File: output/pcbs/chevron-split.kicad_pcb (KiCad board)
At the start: 2 copper layers, 167.5 x 131.1 mm, 132 parts

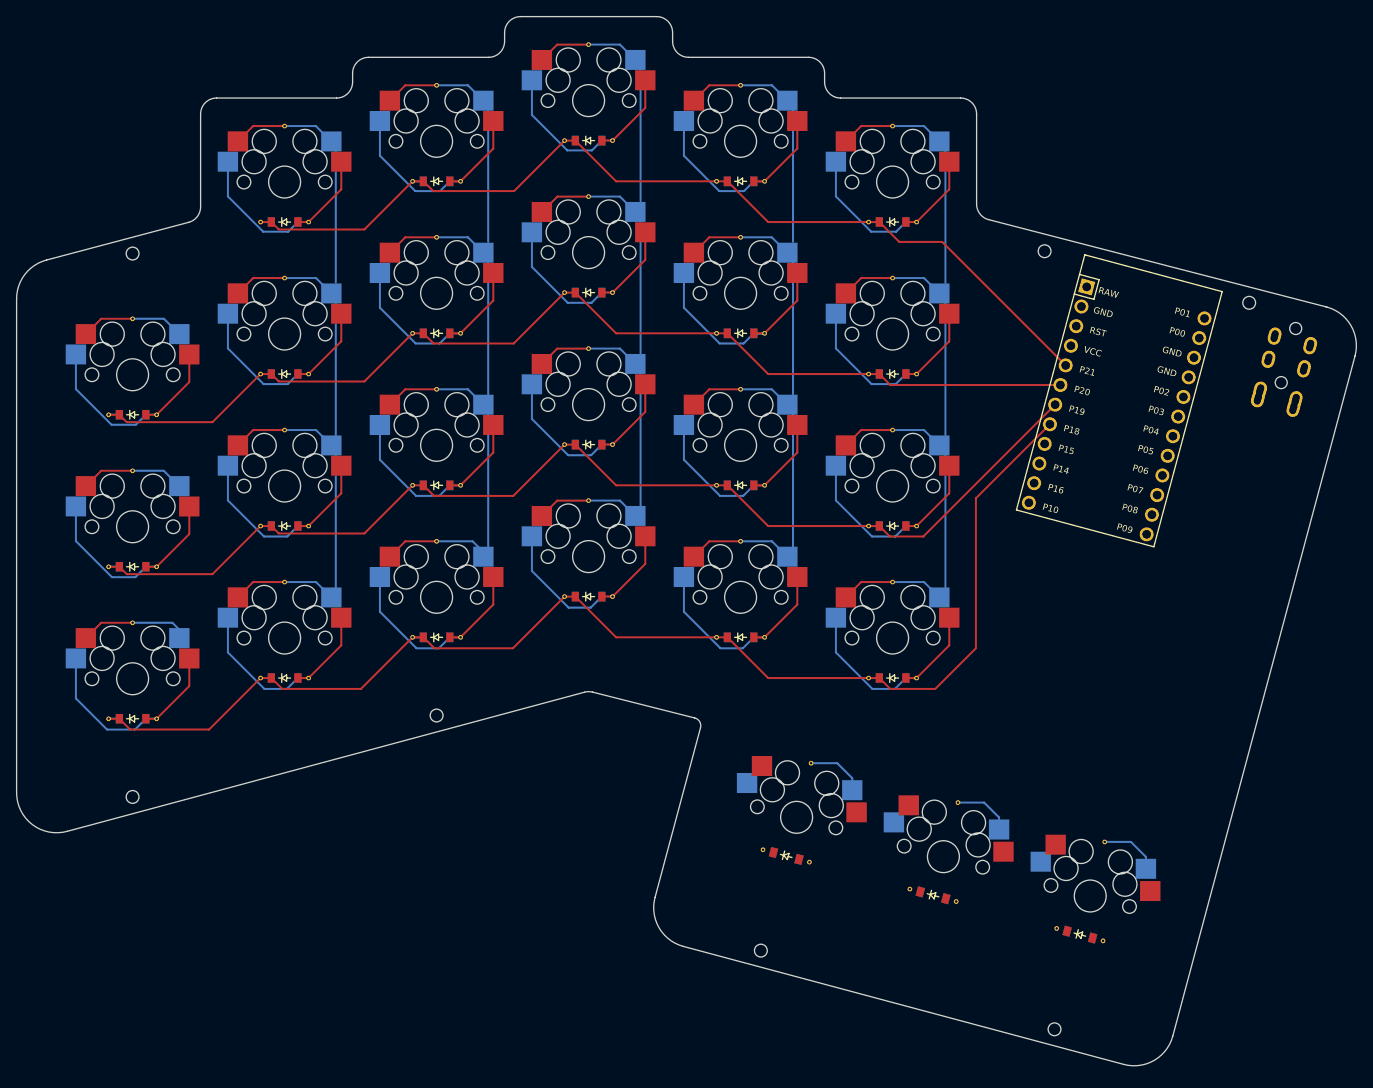
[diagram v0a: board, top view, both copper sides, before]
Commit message: Snapshot of files for manufacturing prototype version 0.1 PCBs. Created left and right versions for faster prototype iteration.
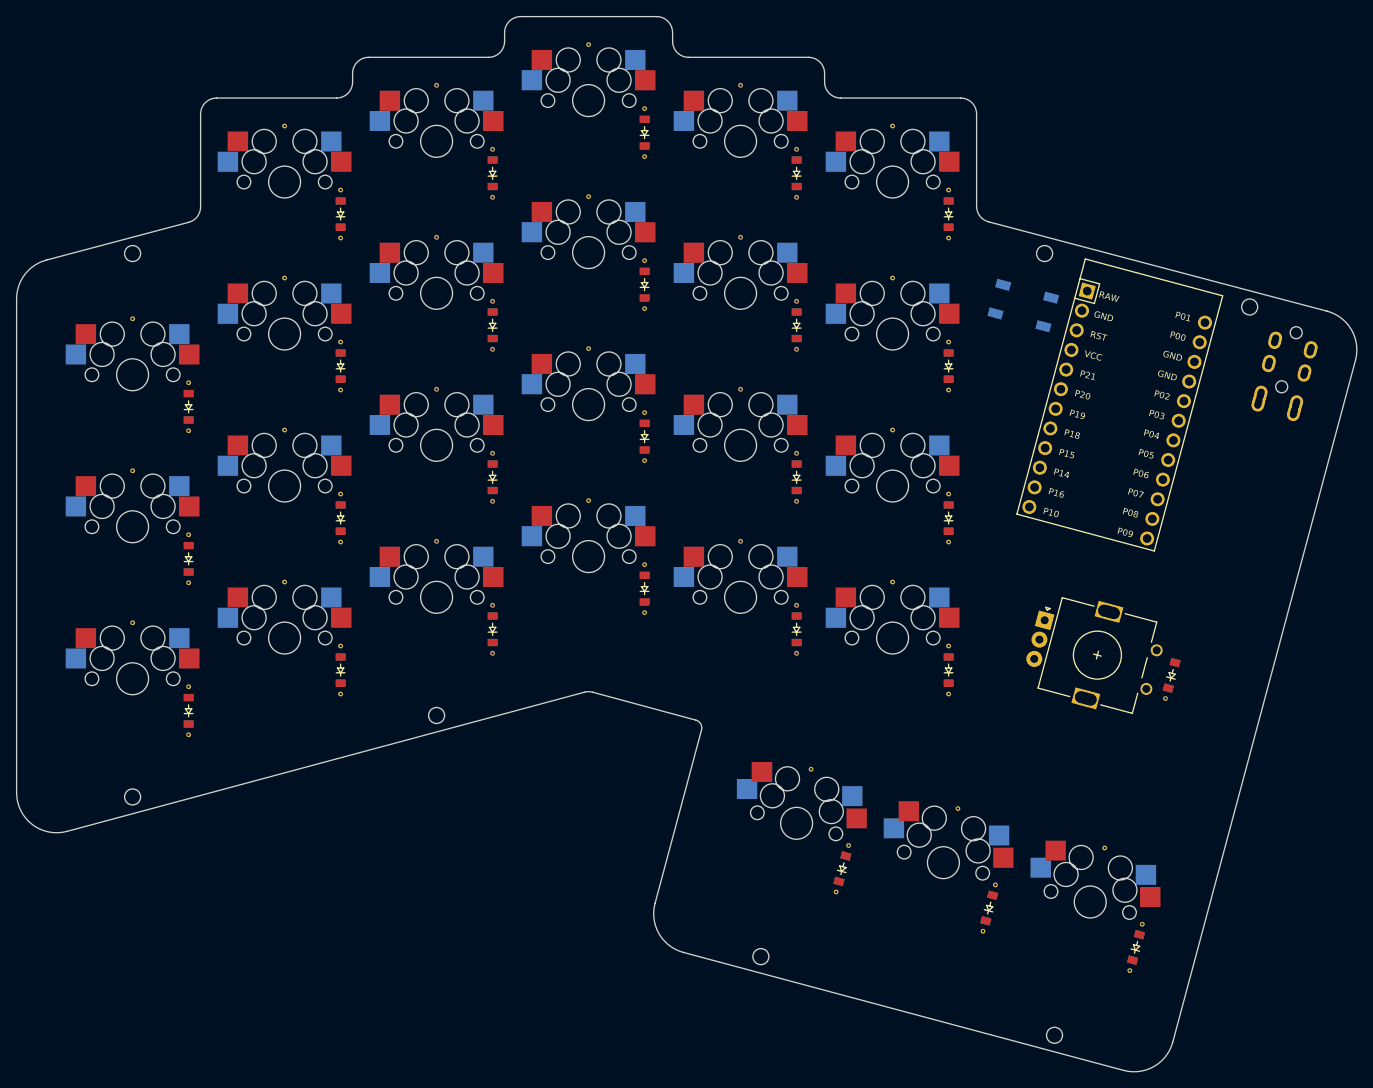
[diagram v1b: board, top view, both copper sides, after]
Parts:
- removed the REF** at (54.0, -48.3)
- removed the REF** at (84.6, 22.9)
- removed the REF** at (3.00, -33.0)
- removed the REF** at (35.0, -5.18)
- removed the REF** at (22.0, -38.1)
- removed the REF** at (79.0, -43.2)
- removed the REF** at (97.2, 26.3)
- removed the REF** at (35.0, -62.2)
- removed the REF** at (92.0, -0.09)
- removed the REF** at (79.0, -24.2)
- removed the REF** at (60.0, -48.3)
- removed the REF** at (73.0, -43.2)
- removed the REF** at (92.0, -38.1)
- removed the REF** at (60.0, -10.3)
- removed the REF** at (60.0, -67.3)
- removed the REF** at (22.0, -0.09)
- removed the REF** at (121.3, 32.8)
- removed the REF** at (98.0, -38.1)
- removed the REF** at (92.0, -57.1)
- removed the REF** at (-3.00, -33.0)
- removed the REF** at (41.0, -24.2)
- removed the REF** at (73.0, -24.2)
- removed the REF** at (35.0, -24.2)
- removed the REF** at (35.0, -43.2)
- removed the REF** at (16.0, -38.1)
- removed the REF** at (3.00, 5.00)
- removed the REF** at (73.0, -5.18)
- removed the REF** at (22.0, -57.1)
- removed the REF** at (98.0, -19.1)
- removed the REF** at (103.0, 27.8)
- removed the REF** at (16.0, -57.1)
- removed the REF** at (-3.00, 5.00)
- removed the REF** at (98.0, -0.09)
- removed the REF** at (121.5, 20.4)
- removed the REF** at (103.2, 15.5)
- removed the REF** at (41.0, -43.2)
- removed the REF** at (54.0, -10.3)
- removed the REF** at (-3.00, -14.0)
- removed the REF** at (54.0, -67.3)
- removed the REF** at (60.0, -29.3)
- removed the REF** at (115.5, 31.2)
- removed the REF** at (92.0, -19.1)
- removed the REF** at (79.0, -62.2)
- removed the REF** at (73.0, -62.2)
- removed the REF** at (22.0, -19.1)
- removed the REF** at (79.0, -5.18)
- removed the REF** at (98.0, -57.1)
- removed the REF** at (41.0, -5.18)
- removed the REF** at (84.8, 10.6)
- removed the REF** at (16.0, -19.1)
- removed the REF** at (78.8, 21.4)
- removed the REF** at (41.0, -62.2)
- removed the REF** at (16.0, -0.09)
- removed the REF** at (54.0, -29.3)
- removed the REF** at (3.00, -14.0)
- added B1: , E73:SW_TACT_ALPS_SKQGABE010, F.Cu at (111.3, -46.7)
- added D27: , ComboDiode, F.Cu at (129.9, -0.43)
- added REF**: VIA-0.6mm, VIA-0.6mm, F.Cu at (7.00, 1.00)
- added REF**: VIA-0.6mm, VIA-0.6mm, F.Cu at (26.0, -4.09)
- added REF**: VIA-0.6mm, VIA-0.6mm, F.Cu at (26.0, 1.91)
- added REF**: VIA-0.6mm, VIA-0.6mm, F.Cu at (26.0, -23.1)
- added REF**: VIA-0.6mm, VIA-0.6mm, F.Cu at (26.0, -17.1)
- added REF**: VIA-0.6mm, VIA-0.6mm, F.Cu at (26.0, -42.1)
- added REF**: VIA-0.6mm, VIA-0.6mm, F.Cu at (26.0, -36.1)
- added REF**: VIA-0.6mm, VIA-0.6mm, F.Cu at (26.0, -61.1)
- added REF**: VIA-0.6mm, VIA-0.6mm, F.Cu at (7.00, 7.00)
- added REF**: VIA-0.6mm, VIA-0.6mm, F.Cu at (26.0, -55.1)
- added REF**: VIA-0.6mm, VIA-0.6mm, F.Cu at (45.0, -9.18)
- added REF**: VIA-0.6mm, VIA-0.6mm, F.Cu at (45.0, -3.18)
- added REF**: VIA-0.6mm, VIA-0.6mm, F.Cu at (45.0, -28.2)
- added REF**: VIA-0.6mm, VIA-0.6mm, F.Cu at (45.0, -22.2)
- added REF**: VIA-0.6mm, VIA-0.6mm, F.Cu at (45.0, -47.2)
- added REF**: VIA-0.6mm, VIA-0.6mm, F.Cu at (45.0, -41.2)
- added REF**: VIA-0.6mm, VIA-0.6mm, F.Cu at (45.0, -66.2)
- added REF**: VIA-0.6mm, VIA-0.6mm, F.Cu at (45.0, -60.2)
- added REF**: VIA-0.6mm, VIA-0.6mm, F.Cu at (64.0, -14.3)
- added REF**: VIA-0.6mm, VIA-0.6mm, F.Cu at (64.0, -8.27)
- added REF**: VIA-0.6mm, VIA-0.6mm, F.Cu at (64.0, -33.3)
- added REF**: VIA-0.6mm, VIA-0.6mm, F.Cu at (64.0, -27.3)
- added REF**: VIA-0.6mm, VIA-0.6mm, F.Cu at (7.00, -18.0)
- added REF**: VIA-0.6mm, VIA-0.6mm, F.Cu at (64.0, -52.3)
- added REF**: VIA-0.6mm, VIA-0.6mm, F.Cu at (64.0, -46.3)
- added REF**: VIA-0.6mm, VIA-0.6mm, F.Cu at (64.0, -71.3)
- added REF**: VIA-0.6mm, VIA-0.6mm, F.Cu at (64.0, -65.3)
- added REF**: VIA-0.6mm, VIA-0.6mm, F.Cu at (83.0, -9.18)
- added REF**: VIA-0.6mm, VIA-0.6mm, F.Cu at (83.0, -3.18)
- added REF**: VIA-0.6mm, VIA-0.6mm, F.Cu at (83.0, -28.2)
- added REF**: VIA-0.6mm, VIA-0.6mm, F.Cu at (7.00, -12.0)
- added REF**: VIA-0.6mm, VIA-0.6mm, F.Cu at (83.0, -22.2)
- added REF**: VIA-0.6mm, VIA-0.6mm, F.Cu at (83.0, -47.2)
- added REF**: VIA-0.6mm, VIA-0.6mm, F.Cu at (83.0, -41.2)
- added REF**: VIA-0.6mm, VIA-0.6mm, F.Cu at (83.0, -66.2)
- added REF**: VIA-0.6mm, VIA-0.6mm, F.Cu at (83.0, -60.2)
- added REF**: VIA-0.6mm, VIA-0.6mm, F.Cu at (102.0, -4.09)
- added REF**: VIA-0.6mm, VIA-0.6mm, F.Cu at (102.0, 1.91)
- added REF**: VIA-0.6mm, VIA-0.6mm, F.Cu at (102.0, -23.1)
- added REF**: VIA-0.6mm, VIA-0.6mm, F.Cu at (102.0, -17.1)
- added REF**: VIA-0.6mm, VIA-0.6mm, F.Cu at (102.0, -42.1)
- added REF**: VIA-0.6mm, VIA-0.6mm, F.Cu at (102.0, -36.1)
- added REF**: VIA-0.6mm, VIA-0.6mm, F.Cu at (102.0, -61.1)
- added REF**: VIA-0.6mm, VIA-0.6mm, F.Cu at (102.0, -55.1)
- added REF**: VIA-0.6mm, VIA-0.6mm, F.Cu at (7.00, -37.0)
- added REF**: VIA-0.6mm, VIA-0.6mm, F.Cu at (89.5, 20.8)
- added REF**: VIA-0.6mm, VIA-0.6mm, F.Cu at (87.9, 26.6)
- added REF**: VIA-0.6mm, VIA-0.6mm, F.Cu at (84.8, 11.3)
- added REF**: VIA-0.6mm, VIA-0.6mm, F.Cu at (107.9, 25.8)
- added REF**: VIA-0.6mm, VIA-0.6mm, F.Cu at (106.3, 31.6)
- added REF**: VIA-0.6mm, VIA-0.6mm, F.Cu at (103.2, 16.2)
- added REF**: VIA-0.6mm, VIA-0.6mm, F.Cu at (126.2, 30.7)
- added REF**: VIA-0.6mm, VIA-0.6mm, F.Cu at (124.7, 36.5)
- added REF**: VIA-0.6mm, VIA-0.6mm, F.Cu at (121.5, 21.1)
- added REF**: VIA-0.6mm, VIA-0.6mm, F.Cu at (7.00, -31.0)
- added REF**: VIA-0.6mm, VIA-0.6mm, F.Cu at (129.1, 2.47)
- added ROT1: , rotary_encoder, F.Cu at (120.7, -2.88)
- moved D26 7.20 mm to (125.4, 33.6), turned to 75 degrees
- moved D24 7.20 mm to (88.7, 23.7), turned to 75 degrees
- moved D25 7.20 mm to (107.1, 28.7), turned to 75 degrees
- moved D1 7.07 mm to (7.00, 4.00), turned to 90 degrees
- moved D10 7.07 mm to (45.0, -44.2), turned to 90 degrees
- moved D11 7.07 mm to (45.0, -63.2), turned to 90 degrees
- moved D12 7.07 mm to (64.0, -11.3), turned to 90 degrees
- moved D13 7.07 mm to (64.0, -30.3), turned to 90 degrees
- moved D14 7.07 mm to (64.0, -49.3), turned to 90 degrees
- moved D15 7.07 mm to (64.0, -68.3), turned to 90 degrees
- moved D16 7.07 mm to (83.0, -6.18), turned to 90 degrees
- moved D17 7.07 mm to (83.0, -25.2), turned to 90 degrees
- moved D18 7.07 mm to (83.0, -44.2), turned to 90 degrees
- moved D19 7.07 mm to (83.0, -63.2), turned to 90 degrees
- moved D2 7.07 mm to (7.00, -15.0), turned to 90 degrees
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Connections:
- D1 pad 1: P18 -> P15
- D10 pad 1: P20 -> P16
- D11 pad 1: P21 -> P10
- D12 pad 1: P18 -> P15
- D13 pad 1: P19 -> P14
- D14 pad 1: P20 -> P16
- D15 pad 1: P21 -> P10
- D16 pad 1: P18 -> P15
- D17 pad 1: P19 -> P14
- D18 pad 1: P20 -> P16
- D19 pad 1: P21 -> P10
- D2 pad 1: P19 -> P14
- D20 pad 1: P18 -> P15
- D21 pad 1: P19 -> P14
- D22 pad 1: P20 -> P16
- D23 pad 1: P21 -> P10
- D24 pad 1: P9 -> P18
- D25 pad 1: P9 -> P18
- D26 pad 1: P9 -> P18
- D3 pad 1: P20 -> P16
- D4 pad 1: P18 -> P15
- D5 pad 1: P19 -> P14
- D6 pad 1: P20 -> P16
- D7 pad 1: P21 -> P10
- D8 pad 1: P18 -> P15
- D9 pad 1: P19 -> P14
- REF** pad 1: P4 -> P8 (x4)
- REF** pad 1: P5 -> P7 (x4)
- REF** pad 1: P4 -> P9 (x3)
- REF** pad 1: P7 -> P5 (x4)
- REF** pad 1: P8 -> P4 (x4)
- S1 pad 2: P4 -> P9
- S10 pad 2: P5 -> P7
- S11 pad 2: P5 -> P7
- S16 pad 2: P7 -> P5
- S17 pad 2: P7 -> P5
- S18 pad 2: P7 -> P5
- S19 pad 2: P7 -> P5
- S2 pad 2: P4 -> P9
- S20 pad 2: P8 -> P4
- S21 pad 2: P8 -> P4
- S22 pad 2: P8 -> P4
- S23 pad 2: P8 -> P4
- S25 pad 2: P7 -> P5
- S26 pad 2: P8 -> P4
- S3 pad 2: P4 -> P9
- S4 pad 2: P4 -> P8
- S5 pad 2: P4 -> P8
- S6 pad 2: P4 -> P8
- S7 pad 2: P4 -> P8
- S8 pad 2: P5 -> P7
- S9 pad 2: P5 -> P7
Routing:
- net P18: track 162.2 -> 0.00 mm
- net P4: track 147.3 -> 0.00 mm
- net P19: track 142.9 -> 0.00 mm
- net P20: track 136.7 -> 0.00 mm
- net P21: track 122.3 -> 0.00 mm
- net P8: track 114.5 -> 0.00 mm
- net P7: track 114.5 -> 0.00 mm
- net P6: track 114.5 -> 0.00 mm
- net P5: track 107.3 -> 0.00 mm
- net index_upper: track 28.5 -> 0.00 mm
- net outer_lower: track 27.8 -> 0.00 mm
- net middle_lower: track 27.5 -> 0.00 mm
- net ring_lower: track 27.5 -> 0.00 mm
- net index_lower: track 27.5 -> 0.00 mm
- net pinky_lower: track 27.5 -> 0.00 mm
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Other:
- board size 167.5 x 131.1 mm -> 167.5 x 131.9 mm
- net class Default added: clearance 0.2, trace_width 0.25, via_dia 0.8, via_drill 0.4
